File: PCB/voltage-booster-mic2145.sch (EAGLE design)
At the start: 20 parts

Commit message: Ad/update component values.
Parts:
- C1: value (none) -> 10uF/6.3V
- C4: value 10uF -> 10uF/16V
- R2: value 200 -> 470
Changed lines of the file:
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@@
 </classes>
 <parts>
-<part name="SHEET1" library="frames-custom" library_urn="urn:adsk.eagle:library:11820551" deviceset="LETTER_L-CIRCUITMONKEY" device=""/>
+<part name="SHEET1" library="frames-custom" library_urn="urn:adsk.eagle:library:11820551" deviceset="LETTER_L-CIRCUITMONKEY" device="">
+<attribute name="DOCUMENT_NUMBER" value="Boost, Input 3.7V  Output: 9V and -9V"/>
+<attribute name="REV" value="A"/>
+</part>
 <part name="BOOST1" library="regulators" library_urn="urn:adsk.eagle:library:7189770" deviceset="BOOST-MIC2145" device="-MSOP" package3d_urn="urn:adsk.eagle:package:7191701/3" value="MIC2145"/>
 <part name="SUPPLY1" library="supply" library_urn="urn:adsk.eagle:library:10485988" deviceset="GND" device=""/>
-<part name="C1" library="rlc" library_urn="urn:adsk.eagle:library:4192893" deviceset="CAPACITOR" device="0603" package3d_urn="urn:adsk.eagle:package:4193021/2"/>
+<part name="C1" library="rlc" library_urn="urn:adsk.eagle:library:4192893" deviceset="CAPACITOR" device="0603" package3d_urn="urn:adsk.eagle:package:4193021/2" value="10uF/6.3V"/>
 <part name="R1" library="rlc" library_urn="urn:adsk.eagle:library:4192893" deviceset="RESISTOR" device="0603" package3d_urn="urn:adsk.eagle:package:4193040/2" value="100K"/>
 <part name="VIN" library="con-headers" library_urn="urn:adsk.eagle:library:5539071" deviceset="CAST-01X1" device="2.54MM" package3d_urn="urn:adsk.eagle:package:14150085/3"/>
@@
 <part name="D1" library="diodes" library_urn="urn:adsk.eagle:library:7189447" deviceset="SCHOTTKY" device="B140" package3d_urn="urn:adsk.eagle:package:7189483/2" value="B140"/>
 <part name="C2" library="rlc" library_urn="urn:adsk.eagle:library:4192893" deviceset="CAPACITOR" device="0603" package3d_urn="urn:adsk.eagle:package:4193021/2" value="0.01uF"/>
-<part name="R2" library="rlc" library_urn="urn:adsk.eagle:library:4192893" deviceset="RESISTOR" device="0603" package3d_urn="urn:adsk.eagle:package:4193040/2" value="200"/>
+<part name="R2" library="rlc" library_urn="urn:adsk.eagle:library:4192893" deviceset="RESISTOR" device="0603" package3d_urn="urn:adsk.eagle:package:4193040/2" value="470"/>
 <part name="C3" library="rlc" library_urn="urn:adsk.eagle:library:4192893" deviceset="CAPACITOR" device="0603" package3d_urn="urn:adsk.eagle:package:4193021/2" value="100pF"/>
 <part name="R3" library="rlc" library_urn="urn:adsk.eagle:library:4192893" deviceset="RESISTOR" device="0603" package3d_urn="urn:adsk.eagle:package:4193040/2" value="136K"/>
 <part name="R4" library="rlc" library_urn="urn:adsk.eagle:library:4192893" deviceset="RESISTOR" device="0603" package3d_urn="urn:adsk.eagle:package:4193040/2" value="1M"/>
-<part name="C4" library="rlc" library_urn="urn:adsk.eagle:library:4192893" deviceset="CAPACITOR" device="0603" package3d_urn="urn:adsk.eagle:package:4193021/2" value="10uF"/>
+<part name="C4" library="rlc" library_urn="urn:adsk.eagle:library:4192893" deviceset="CAPACITOR" device="0603" package3d_urn="urn:adsk.eagle:package:4193021/2" value="10uF/16V"/>
 <part name="SUPPLY2" library="supply" library_urn="urn:adsk.eagle:library:10485988" deviceset="GND" device=""/>
 <part name="SUPPLY3" library="supply" library_urn="urn:adsk.eagle:library:10485988" deviceset="GND" device=""/>
@@
 <attribute name="SHEET" x="233.68" y="1.27" size="2.54" layer="94" font="vector"/>
 <attribute name="DRAWING_NAME" x="91.44" y="1.27" size="2.54" layer="94" font="vector" ratio="15"/>
+<attribute name="DOCUMENT_NUMBER" x="160.02" y="6.096" size="3.048" layer="94" ratio="15"/>
+<attribute name="REV" x="241.808" y="8.382" size="3.81" layer="94" ratio="15" align="center"/>
 </instance>
 <instance part="BOOST1" gate="G$1" x="71.12" y="114.3" smashed="yes">

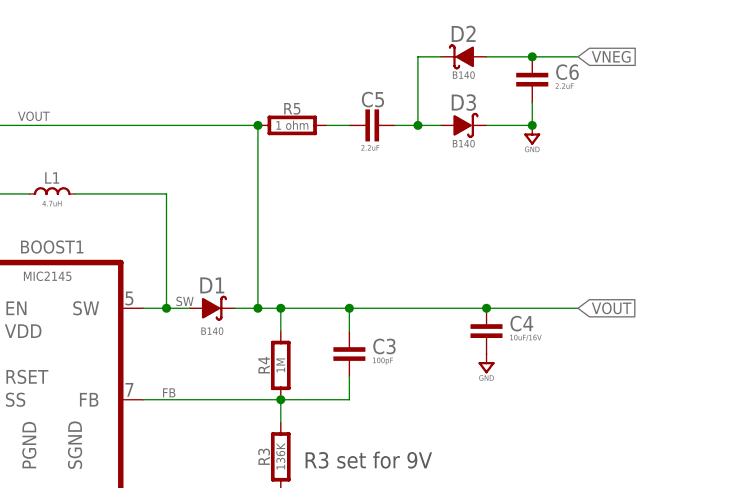
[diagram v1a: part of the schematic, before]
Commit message: Fix error where neg-volt section on wrong signal.
Bumped rev to B
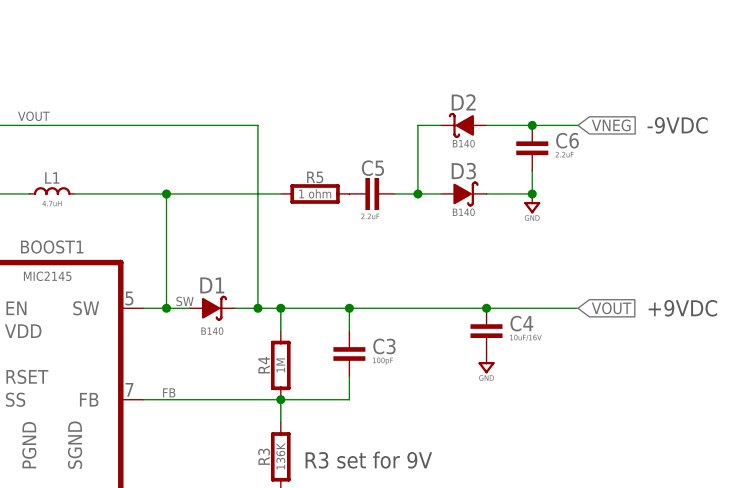
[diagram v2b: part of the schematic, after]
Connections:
- net SW: now also R5.1
- net VOUT: no longer R5.1
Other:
- note added: "+9VDC"
- note added: "-9VDC"
- moved on the sheet: C5, C6, D2, D3, R5
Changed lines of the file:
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@@
 <part name="SHEET1" library="frames-custom" library_urn="urn:adsk.eagle:library:11820551" deviceset="LETTER_L-CIRCUITMONKEY" device="">
 <attribute name="DOCUMENT_NUMBER" value="Boost, Input 3.7V  Output: 9V and -9V"/>
-<attribute name="REV" value="A"/>
+<attribute name="REV" value="B"/>
 </part>
 <part name="BOOST1" library="regulators" library_urn="urn:adsk.eagle:library:7189770" deviceset="BOOST-MIC2145" device="-MSOP" package3d_urn="urn:adsk.eagle:package:7191701/3" value="MIC2145"/>
@@
 <plain>
 <text x="99.06" y="101.6" size="1.778" layer="97">R3 set for 9V</text>
+<text x="137.16" y="139.7" size="1.778" layer="97" align="center-left">-9VDC</text>
+<text x="137.16" y="119.38" size="1.778" layer="97" align="center-left">+9VDC</text>
 </plain>
 <instances>
@@
 <attribute name="VALUE" x="119.38" y="111.633" size="0.6096" layer="96" font="vector" align="center"/>
 </instance>
-<instance part="R5" gate="G$1" x="96.52" y="139.7" smashed="yes">
-<attribute name="NAME" x="97.79" y="140.9192" size="1.27" layer="95" font="vector" ratio="15" align="bottom-center"/>
-<attribute name="VALUE" x="97.79" y="139.7" size="0.9652" layer="96" font="vector" align="center"/>
-</instance>
-<instance part="D2" gate="G$1" x="116.84" y="147.32" smashed="yes" rot="MR0">
-<attribute name="NAME" x="116.84" y="149.86" size="1.778" layer="95" font="vector" ratio="15" rot="MR0" align="center"/>
-<attribute name="VALUE" x="116.84" y="145.288" size="0.8128" layer="96" font="fixed" rot="MR0" align="center"/>
-</instance>
-<instance part="D3" gate="G$1" x="116.84" y="139.7" smashed="yes">
-<attribute name="NAME" x="116.84" y="142.24" size="1.778" layer="95" font="vector" ratio="15" align="center"/>
-<attribute name="VALUE" x="116.84" y="137.668" size="0.8128" layer="96" font="fixed" align="center"/>
-</instance>
-<instance part="C5" gate="G$1" x="106.68" y="139.7" smashed="yes" rot="R90">
-<attribute name="NAME" x="105.41" y="141.732" size="1.6764" layer="95" font="vector" ratio="15"/>
-<attribute name="VALUE" x="105.41" y="136.906" size="0.6096" layer="96" font="vector"/>
-</instance>
-<instance part="SUPPLY9" gate="GND" x="124.46" y="139.7" smashed="yes">
-<attribute name="VALUE" x="124.46" y="137.033" size="0.6096" layer="96" font="vector" align="center"/>
-</instance>
-<instance part="C6" gate="G$1" x="124.46" y="144.78" smashed="yes">
-<attribute name="NAME" x="127" y="144.78" size="1.6764" layer="95" font="vector" ratio="15"/>
-<attribute name="VALUE" x="127" y="143.764" size="0.6096" layer="96" font="vector"/>
+<instance part="R5" gate="G$1" x="99.06" y="132.08" smashed="yes">
+<attribute name="NAME" x="100.33" y="133.2992" size="1.27" layer="95" font="vector" ratio="15" align="bottom-center"/>
+<attribute name="VALUE" x="100.33" y="132.08" size="0.9652" layer="96" font="vector" align="center"/>
+</instance>
+<instance part="D2" gate="G$1" x="116.84" y="139.7" smashed="yes" rot="MR0">
+<attribute name="NAME" x="116.84" y="142.24" size="1.778" layer="95" font="vector" ratio="15" rot="MR0" align="center"/>
+<attribute name="VALUE" x="116.84" y="137.668" size="0.8128" layer="96" font="fixed" rot="MR0" align="center"/>
+</instance>
+<instance part="D3" gate="G$1" x="116.84" y="132.08" smashed="yes">
+<attribute name="NAME" x="116.84" y="134.62" size="1.778" layer="95" font="vector" ratio="15" align="center"/>
+<attribute name="VALUE" x="116.84" y="130.048" size="0.8128" layer="96" font="fixed" align="center"/>
+</instance>
+<instance part="C5" gate="G$1" x="106.68" y="132.08" smashed="yes" rot="R90">
+<attribute name="NAME" x="105.41" y="134.112" size="1.6764" layer="95" font="vector" ratio="15"/>
+<attribute name="VALUE" x="105.41" y="129.286" size="0.6096" layer="96" font="vector"/>
+</instance>
+<instance part="SUPPLY9" gate="GND" x="124.46" y="132.08" smashed="yes">
+<attribute name="VALUE" x="124.46" y="129.413" size="0.6096" layer="96" font="vector" align="center"/>
+</instance>
+<instance part="C6" gate="G$1" x="124.46" y="137.16" smashed="yes">
+<attribute name="NAME" x="127" y="137.16" size="1.6764" layer="95" font="vector" ratio="15"/>
+<attribute name="VALUE" x="127" y="136.144" size="0.6096" layer="96" font="vector"/>
 </instance>
 </instances>
@@
 <pinref part="D3" gate="G$1" pin="K"/>
 <pinref part="SUPPLY9" gate="GND" pin="GND"/>
-<wire x1="124.46" y1="139.7" x2="119.38" y2="139.7" width="0.1524" layer="91"/>
+<wire x1="124.46" y1="132.08" x2="119.38" y2="132.08" width="0.1524" layer="91"/>
 <pinref part="C6" gate="G$1" pin="2"/>
-<wire x1="124.46" y1="142.24" x2="124.46" y2="139.7" width="0.1524" layer="91"/>
-<junction x="124.46" y="139.7"/>
+<wire x1="124.46" y1="134.62" x2="124.46" y2="132.08" width="0.1524" layer="91"/>
+<junction x="124.46" y="132.08"/>
 </segment>
 <segment>
@@
 <junction x="83.82" y="119.38"/>
 <label x="84.836" y="119.634" size="1.016" layer="95"/>
+<pinref part="R5" gate="G$1" pin="1"/>
+<wire x1="96.52" y1="132.08" x2="83.82" y2="132.08" width="0.1524" layer="91"/>
+<junction x="83.82" y="132.08"/>
 </segment>
 </net>
@@
 <junction x="93.98" y="119.38"/>
 <wire x1="93.98" y1="119.38" x2="93.98" y2="139.7" width="0.1524" layer="91"/>
+<pinref part="BOOST1" gate="G$1" pin="EN"/>
 <wire x1="93.98" y1="139.7" x2="48.26" y2="139.7" width="0.1524" layer="91"/>
-<pinref part="BOOST1" gate="G$1" pin="EN"/>
 <wire x1="60.96" y1="119.38" x2="53.34" y2="119.38" width="0.1524" layer="91"/>
 <pinref part="R1" gate="G$1" pin="2"/>
@@
 <junction x="119.38" y="119.38"/>
 <label x="129.54" y="119.38" size="1.27" layer="95" xref="yes"/>
-<pinref part="R5" gate="G$1" pin="1"/>
-<junction x="93.98" y="139.7"/>
 </segment>
 <segment>
@@
 <pinref part="R5" gate="G$1" pin="2"/>
 <pinref part="C5" gate="G$1" pin="1"/>
-<wire x1="104.14" y1="139.7" x2="101.6" y2="139.7" width="0.1524" layer="91"/>
 </segment>
 </net>
@@
 <pinref part="C5" gate="G$1" pin="2"/>
 <pinref part="D3" gate="G$1" pin="A"/>
-<wire x1="114.3" y1="139.7" x2="111.76" y2="139.7" width="0.1524" layer="91"/>
-<wire x1="111.76" y1="139.7" x2="109.22" y2="139.7" width="0.1524" layer="91"/>
-<wire x1="111.76" y1="139.7" x2="111.76" y2="147.32" width="0.1524" layer="91"/>
-<junction x="111.76" y="139.7"/>
+<wire x1="114.3" y1="132.08" x2="111.76" y2="132.08" width="0.1524" layer="91"/>
+<wire x1="111.76" y1="132.08" x2="109.22" y2="132.08" width="0.1524" layer="91"/>
+<wire x1="111.76" y1="132.08" x2="111.76" y2="139.7" width="0.1524" layer="91"/>
+<junction x="111.76" y="132.08"/>
 <pinref part="D2" gate="G$1" pin="K"/>
-<wire x1="111.76" y1="147.32" x2="114.3" y2="147.32" width="0.1524" layer="91"/>
+<wire x1="111.76" y1="139.7" x2="114.3" y2="139.7" width="0.1524" layer="91"/>
 </segment>
 </net>
@@
 <pinref part="D2" gate="G$1" pin="A"/>
 <pinref part="C6" gate="G$1" pin="1"/>
-<wire x1="124.46" y1="147.32" x2="119.38" y2="147.32" width="0.1524" layer="91"/>
-<wire x1="124.46" y1="147.32" x2="129.54" y2="147.32" width="0.1524" layer="91"/>
-<junction x="124.46" y="147.32"/>
-<label x="129.54" y="147.32" size="1.27" layer="95" xref="yes"/>
-</segment>
-<segment>
+<wire x1="124.46" y1="139.7" x2="119.38" y2="139.7" width="0.1524" layer="91"/>
+<wire x1="124.46" y1="139.7" x2="129.54" y2="139.7" width="0.1524" layer="91"/>
+<junction x="124.46" y="139.7"/>
+<label x="129.54" y="139.7" size="1.27" layer="95" xref="yes"/>
+</segment>
+<segment>

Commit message: Added schematic notes.
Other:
- note added: "1n4148 on output to balance neg diode drop."
- note added: "Change R2 to 10K"
- note added: "Change to 0.5ohm"
- note added: "Change to 10uH"
- note added: "Higher value 10uF"
- note added: "Put a trim pot here."
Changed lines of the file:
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@@
 <text x="137.16" y="139.7" size="1.778" layer="97" align="center-left">-9VDC</text>
 <text x="137.16" y="119.38" size="1.778" layer="97" align="center-left">+9VDC</text>
+<text x="101.6" y="99.06" size="1.778" layer="97">Put a trim pot here.</text>
+<text x="66.04" y="134.62" size="1.778" layer="97">Change to 10uH</text>
+<text x="99.06" y="137.16" size="1.778" layer="97">Change to
+0.5ohm</text>
+<text x="104.14" y="124.46" size="1.778" layer="97">Higher value
+10uF</text>
+<text x="147.32" y="114.3" size="1.778" layer="97">1n4148 on
+output to
+balance neg
+diode drop.</text>
+<text x="45.72" y="86.36" size="1.778" layer="97">Change R2
+to 10K</text>
 </plain>
 <instances>
@@
 </drawing>
 <compatibility>
+<note version="6.3" minversion="6.2.2" severity="warning">
+Since Version 6.2.2 text objects can contain more than one line,
+which will not be processed correctly with this version.
+</note>
 <note version="8.2" severity="warning">
 Since Version 8.2, EAGLE supports online libraries. The ids
